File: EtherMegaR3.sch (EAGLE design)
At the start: 120 parts, among them IC1 EUP3476SO08T, IC2 APX811-44UG-7, IC3 ATMEGA16U2-MU, IC4 MCP24AA025E48, IC6 W5100SQFP80, IC9 ATMEGA2560-16AU, J1 DC_2_1MM, P1 USB-6PSMT, P3 ICSP:USB, P4 microSD, Q2 2N7002, Q3 2N7002, U1 HY931147C-RJ45, X1 16MHz, X2 25MHz, X3 16MHz

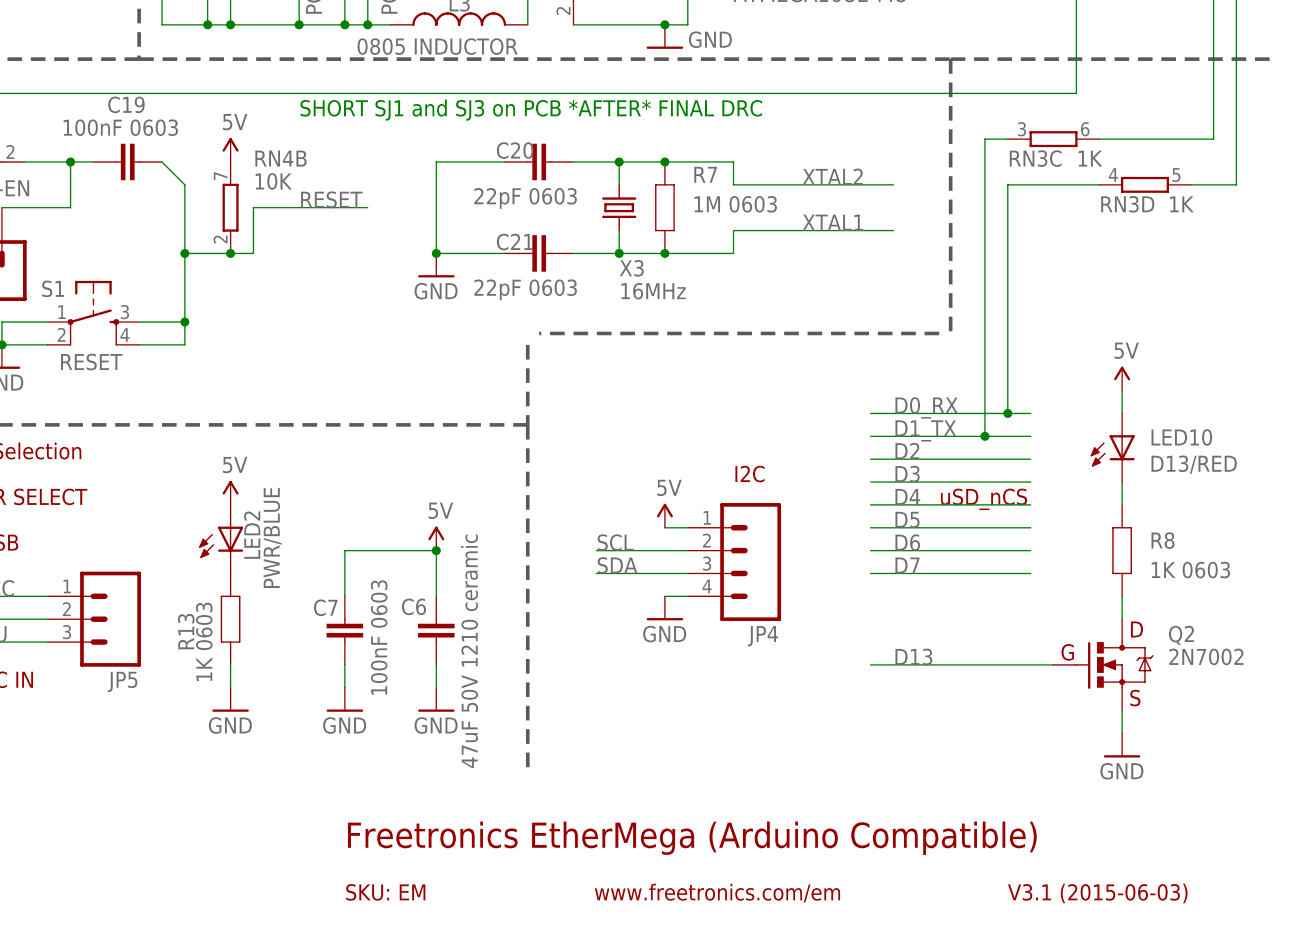
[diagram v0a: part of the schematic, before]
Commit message: Changed branding to SuperHouse for v3.1 release
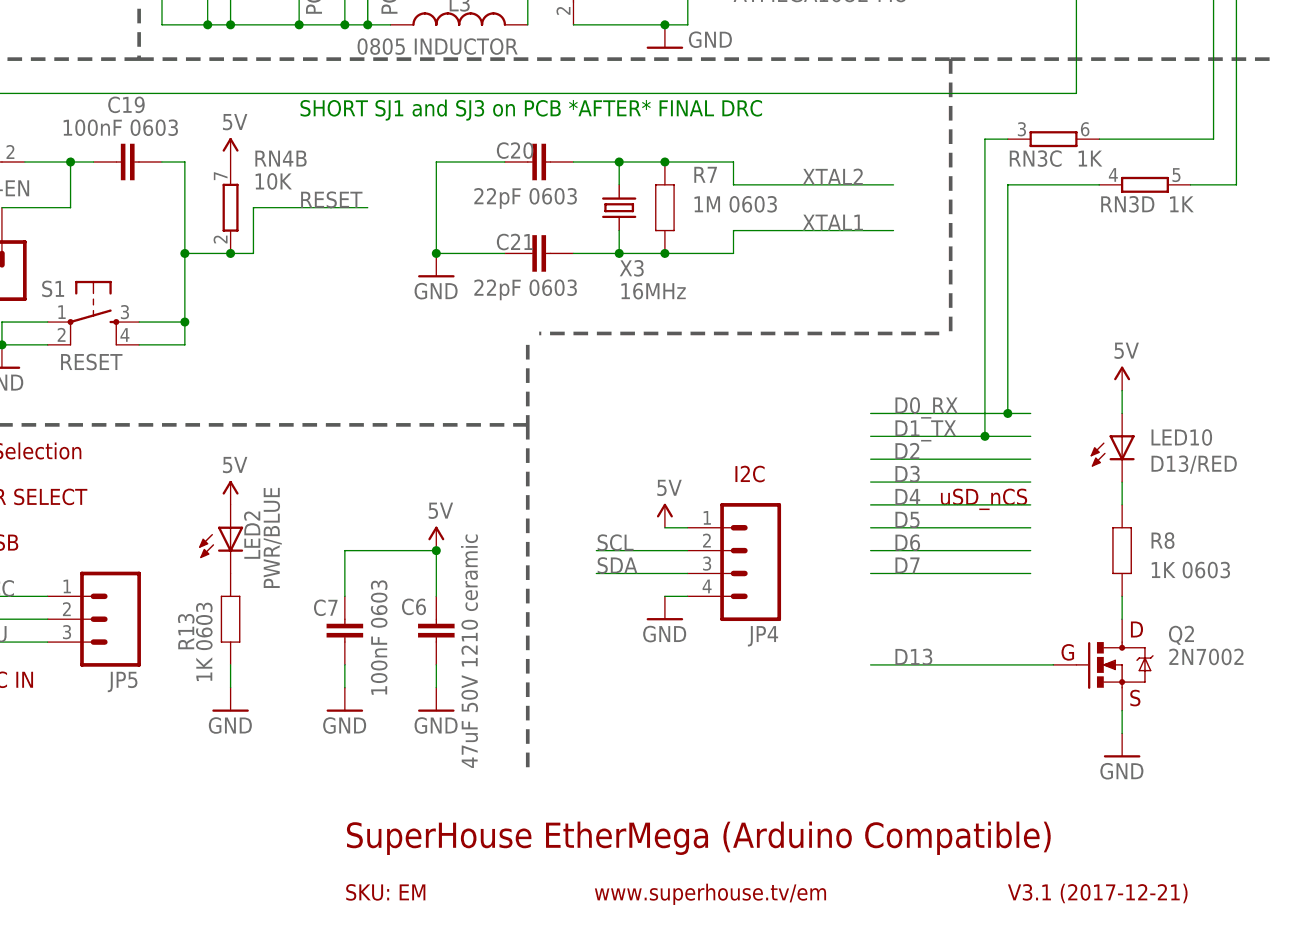
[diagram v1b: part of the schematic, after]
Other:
- note added: "SuperHouse EtherMega (Arduino Compatible)"
- note added: "V3.1 (2017-12-21)"
- note added: "www.superhouse.tv/em"
- note removed: "Freetronics EtherMega (Arduino Compatible)"
- note removed: "V3.1 (2015-06-03)"
- note removed: "www.freetronics.com/em"
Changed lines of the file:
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@@
 <?xml version="1.0" encoding="utf-8"?>
 <!DOCTYPE eagle SYSTEM "eagle.dtd">
-<eagle version="6.5.0">
+<eagle version="8.5.1">
 <drawing>
 <settings>
-<setting alwaysvectorfont="yes"/>
+<setting alwaysvectorfont="no"/>
+<setting keepoldvectorfont="yes"/>
 <setting verticaltext="up"/>
 </settings>
@@
 <text x="261.62" y="96.52" size="1.778" layer="94">In Circuit Serial Programming</text>
 <text x="261.62" y="48.26" size="1.778" layer="94">micro SD Card Slot</text>
-<text x="396.24" y="12.7" size="2.794" layer="94">Freetronics EtherMega (Arduino Compatible)</text>
-<text x="469.9" y="6.858" size="1.778" layer="94">V3.1 (2015-06-03)</text>
-<text x="423.926" y="6.858" size="1.778" layer="94">www.freetronics.com/em</text>
+<text x="396.24" y="12.7" size="2.794" layer="94">SuperHouse EtherMega (Arduino Compatible)</text>
+<text x="469.9" y="6.858" size="1.778" layer="94">V3.1 (2017-12-21)</text>
+<text x="423.926" y="6.858" size="1.778" layer="94">www.superhouse.tv/em</text>
 <text x="396.24" y="6.858" size="1.778" layer="94">SKU: EM</text>
 <text x="7.62" y="106.68" size="1.778" layer="94">Ethernet Module with PoE</text>
@@
 <wire x1="398.78" y1="83.82" x2="386.08" y2="83.82" width="0.1524" layer="91"/>
 <wire x1="386.08" y1="83.82" x2="386.08" y2="78.74" width="0.1524" layer="91"/>
-<wire x1="375.92" y1="88.9" x2="378.46" y2="86.36" width="0.1524" layer="91"/>
-<wire x1="378.46" y1="86.36" x2="378.46" y2="78.74" width="0.1524" layer="91"/>
+<wire x1="375.92" y1="88.9" x2="378.46" y2="88.9" width="0.1524" layer="91"/>
+<wire x1="378.46" y1="88.9" x2="378.46" y2="78.74" width="0.1524" layer="91"/>
 <wire x1="378.46" y1="68.58" x2="378.46" y2="71.12" width="0.1524" layer="91"/>
 <wire x1="378.46" y1="71.12" x2="378.46" y2="78.74" width="0.1524" layer="91"/>

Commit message: Part replacement using SuperHouse libraries
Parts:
- ADCH1, ADCL1, COMMUNICATION1, PWML1: value (none) -> M08-SOCKET; device freetronics-master-v1.1:M08STD -> SuperHouse-Connectors:M08-SOCKET
- C1, C12, C15, C16, C17, C19, C2, C20, C21, C22, C23, C24, C25, C26, C27, C28, C29, C30, C31, C32, C33, C34, C35, C7, C8, C9: device freetronics-marc:CAP0603 -> SuperHouse-DiscreteSemi:CAP0603
- C11: device freetronics-master-v1:CAP0603 -> SuperHouse-DiscreteSemi:CAP0603
- C13, C3, C4: device freetronics:CAP_POL1206 -> SuperHouse-DiscreteSemi:CAP_POL1206
- F1: device rcl:L-EUL1812 -> SuperHouse-Fuses:PTC050
- IC3: device freetronics-jon:ATMEL_ATMEGA8U2-MUQFN -> SuperHouse-MCUs:ATMEGA8U2QFN
- IC6: device freetronics-marc:W5100SQFP80 -> SuperHouse-ICs:W5100SQFP80
- J1: device freetronics:POWER_JACKPTH -> SuperHouse-Connectors:POWER_JACK-SLOTS
- JP5: device freetronics-master-v1.1:M03PTH -> SuperHouse-Connectors:M03-PIN
- LED1, LED10, LED2, LED3, LED4, LED5, LED6, LED7, LED8, LED9: device freetronics-jon:LED0603 -> SuperHouse-LEDs:LED0603
- P1: value USB-6PSMT -> USB-6P-SMT; device freetronics-jon:USB-6PSMT -> SuperHouse-Connectors:USB-6P-SMT
- Q2, Q3: device freetronics:MOSFET-NCHANNELSMD -> SuperHouse-DiscreteSemi:MOSFET-NCHANNEL-233
- R1, R13, R2, R3, R4, R5, R6, R7, R8: device freetronics-marc:RESISTOR0603 -> SuperHouse-DiscreteSemi:RESISTOR0603
- R10, R11, R9: device freetronics-original:RESISTOR0603 -> SuperHouse-DiscreteSemi:RESISTOR0603
- R14, R15: device freetronics-master-v1.1:RESISTOR0603 -> SuperHouse-DiscreteSemi:RESISTOR0603
- REG2: device freetronics:V_REG_LM1117SOT223 -> SuperHouse-Regulators:LD1117
- RN1, RN2, RN3, RN5, RN6, RN7, RN8: device freetronics-master-v1:4R-NCAY16 -> SuperHouse-DiscreteSemi:4R-NCAY16
- S1: device freetronics:TAC_SWITCHSMD -> SuperHouse-Switches:TAC_SWITCH-SMT-6
- U1: device freetronics-jon:HY931147C-RJ45 -> SuperHouse-Connectors:HY931147C-RJ45
- X1, X2, X3: device freetronics-master-v1:CRYSTALHC49UV -> SuperHouse-Oscillators:CRYSTALHC49UV
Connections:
- net 3V3D: no longer REG2.OUT@1
- net GND: now also REG2.GND; no longer REG2.ADJ
